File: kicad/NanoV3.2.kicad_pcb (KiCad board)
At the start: 2 copper layers, 43.2 x 17.8 mm, 24 parts, among them IC2 LM1117IMPX-5.0, IC3 ATMEGA328P-AU, P1 TTL, P2 OUT, P3 INPUT, Q1 s9014, Y1 16MHz

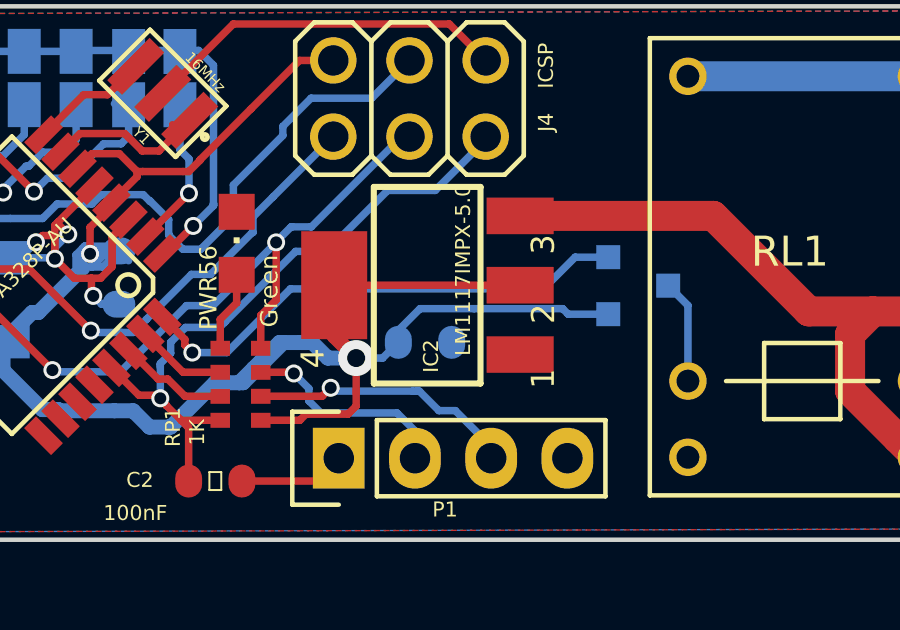
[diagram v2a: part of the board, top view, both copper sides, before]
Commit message: fixed a bug with the transistor
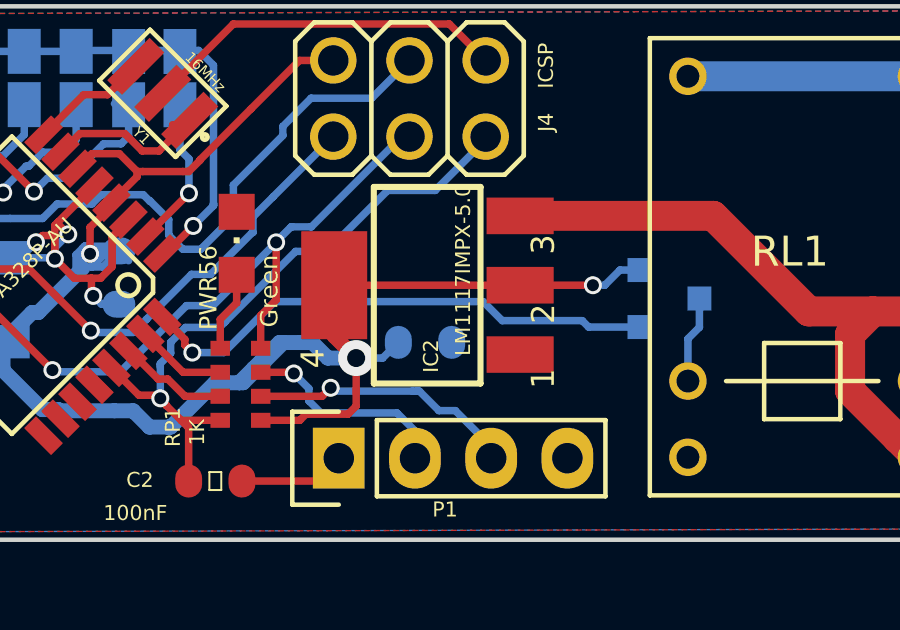
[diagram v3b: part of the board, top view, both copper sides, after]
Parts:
- Q1: value s9014 -> SS8050
- moved Q1 1.13 mm to (155.3, 105.9)
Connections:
- IC3 pad 14: /D10 -> (no net)
- IC3 pad 19: /A6 -> (no net)
- IC3 pad 22: /A7 -> (no net)
- IC3 pad 23: /A0 -> (no net)
- IC3 pad 24: /A1 -> (no net)
- IC3 pad 25: /A2 -> (no net)
- IC3 pad 26: /A3 -> (no net)
- IC3 pad 27: /A4 -> (no net)
- IC3 pad 28: /A5 -> (no net)
- Q1 pad 1: +5V -> /D2
- Q1 pad 2: /D2 -> +5V
- RL1 pad 12: Net-(RL1-Pad12) -> (no net)
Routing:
- net +5V: track 72.9 -> 69.8 mm, vias 3 -> 4
- net /D2: track 17.0 -> 17.7 mm
- net Net-(Q1-Pad3): track 3.45 -> 2.91 mm
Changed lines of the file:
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@@
     (thickness 1.6)
     (drawings 91)
-    (tracks 405)
+    (tracks 409)
     (zones 0)
     (modules 24)
-    (nets 37)
+    (nets 27)
   )
   (page A4)
@@
   (net 25 "Net-(C2-Pad2)")
   (net 26 /RX)
-  (net 27 /D10)
-  (net 28 /A6)
-  (net 29 /A7)
-  (net 30 /A0)
-  (net 31 /A1)
-  (net 32 /A2)
-  (net 33 /A3)
-  (net 34 /A4)
-  (net 35 /A5)
-  (net 36 "Net-(RL1-Pad12)")
   (net_class Default "This is the default net class."
     (clearance 0.2)
@@
     (uvia_drill 0.1)
     (add_net +5V)
-    (add_net /A0)
-    (add_net /A1)
-    (add_net /A2)
-    (add_net /A3)
-    (add_net /A4)
-    (add_net /A5)
-    (add_net /A6)
-    (add_net /A7)
     (add_net /AREF)
     (add_net /D0/RX)
     (add_net /D1/TX)
-    (add_net /D10)
     (add_net /D11/MOSI)
     (add_net /D12/MISO)
@@
     (add_net "Net-(C2-Pad2)")
     (add_net "Net-(Q1-Pad3)")
-    (add_net "Net-(RL1-Pad12)")
   )
   (net_class w0.5 ""
@@
     (pad 13 smd rect (at 0.4 4.2926 225) (size 0.5588 1.27) (layers Top F.Paste F.Mask)
       (net 21 /D9))
-    (pad 14 smd rect (at 1.2 4.2926 225) (size 0.5588 1.27) (layers Top F.Paste F.Mask)
-      (net 27 /D10))
+    (pad 14 smd rect (at 1.2 4.2926 225) (size 0.5588 1.27) (layers Top F.Paste F.Mask))
     (pad 15 smd rect (at 2 4.2926 225) (size 0.5588 1.27) (layers Top F.Paste F.Mask)
       (net 8 /D11/MOSI))
@@
     (pad 18 smd rect (at 4.2926 2 225) (size 1.27 0.5588) (layers Top F.Paste F.Mask)
       (net 2 +5V))
-    (pad 19 smd rect (at 4.2926 1.2 225) (size 1.27 0.5588) (layers Top F.Paste F.Mask)
-      (net 28 /A6))
+    (pad 19 smd rect (at 4.2926 1.2 225) (size 1.27 0.5588) (layers Top F.Paste F.Mask))
     (pad 20 smd rect (at 4.2926 0.4 225) (size 1.27 0.5588) (layers Top F.Paste F.Mask)
       (net 3 /AREF))
     (pad 21 smd rect (at 4.2926 -0.4 225) (size 1.27 0.5588) (layers Top F.Paste F.Mask)
       (net 1 COM))
-    (pad 22 smd rect (at 4.2926 -1.2 225) (size 1.27 0.5588) (layers Top F.Paste F.Mask)
-      (net 29 /A7))
-    (pad 23 smd rect (at 4.2926 -2 225) (size 1.27 0.5588) (layers Top F.Paste F.Mask)
-      (net 30 /A0))
-    (pad 24 smd rect (at 4.2926 -2.8 225) (size 1.27 0.5588) (layers Top F.Paste F.Mask)
-      (net 31 /A1))
-    (pad 25 smd rect (at 2.8 -4.2926 225) (size 0.5588 1.27) (layers Top F.Paste F.Mask)
-      (net 32 /A2))
-    (pad 26 smd rect (at 2 -4.2926 225) (size 0.5588 1.27) (layers Top F.Paste F.Mask)
-      (net 33 /A3))
-    (pad 27 smd rect (at 1.2 -4.2926 225) (size 0.5588 1.27) (layers Top F.Paste F.Mask)
-      (net 34 /A4))
-    (pad 28 smd rect (at 0.4 -4.2926 225) (size 0.5588 1.27) (layers Top F.Paste F.Mask)
-      (net 35 /A5))
+    (pad 22 smd rect (at 4.2926 -1.2 225) (size 1.27 0.5588) (layers Top F.Paste F.Mask))
+    (pad 23 smd rect (at 4.2926 -2 225) (size 1.27 0.5588) (layers Top F.Paste F.Mask))
+    (pad 24 smd rect (at 4.2926 -2.8 225) (size 1.27 0.5588) (layers Top F.Paste F.Mask))
+    (pad 25 smd rect (at 2.8 -4.2926 225) (size 0.5588 1.27) (layers Top F.Paste F.Mask))
+    (pad 26 smd rect (at 2 -4.2926 225) (size 0.5588 1.27) (layers Top F.Paste F.Mask))
+    (pad 27 smd rect (at 1.2 -4.2926 225) (size 0.5588 1.27) (layers Top F.Paste F.Mask))
+    (pad 28 smd rect (at 0.4 -4.2926 225) (size 0.5588 1.27) (layers Top F.Paste F.Mask))
     (pad 29 smd rect (at -0.4 -4.2926 225) (size 0.5588 1.27) (layers Top F.Paste F.Mask)
       (net 4 /RESET))
@@
     (pad A2 thru_hole circle (at 2.54 0 90) (size 1.25 1.25) (drill 0.762) (layers *.Cu *.Mask)
       (net 1 COM))
-    (pad 12 thru_hole circle (at 0 -7.62 90) (size 1.25 1.25) (drill 0.762) (layers *.Cu *.Mask)
-      (net 36 "Net-(RL1-Pad12)"))
+    (pad 12 thru_hole circle (at 0 -7.62 90) (size 1.25 1.25) (drill 0.762) (layers *.Cu *.Mask))
     (pad 14 thru_hole circle (at 0 0 90) (size 1.25 1.25) (drill 0.762) (layers *.Cu *.Mask)
       (net 14 VIN))
@@
   )
   (module TO_SOT_Packages_SMD:SOT-23 (layer Bottom)
-    (at 154.2288 105.42524 90)
+    (at 155.2702 105.8545 90)
     (descr "SOT-23, Standard")
     (tags SOT-23)
@@
       (effects (font (size 0.5 0.5) (thickness 0.1)) (justify mirror))
     )
-    (fp_text value s9014 (at 3.2766 -0.2794 180) (layer B.Fab)
+    (fp_text value SS8050 (at 3.2766 -0.2794 180) (layer B.Fab)
       (effects (font (size 0.5 0.5) (thickness 0.1)) (justify mirror))
     )
@@
     (fp_line (start 1.49982 0.65024) (end 1.49982 -0.0508) (layer B.SilkS) (width 0.15))
     (pad 1 smd rect (at -0.95 -1.00076 90) (size 0.8001 0.8001) (layers Bottom B.Paste B.Mask)
+      (net 22 /D2))
+    (pad 2 smd rect (at 0.95 -1.00076 90) (size 0.8001 0.8001) (layers Bottom B.Paste B.Mask)
       (net 2 +5V))
-    (pad 2 smd rect (at 0.95 -1.00076 90) (size 0.8001 0.8001) (layers Bottom B.Paste B.Mask)
-      (net 22 /D2))
     (pad 3 smd rect (at 0 0.99822 90) (size 0.8001 0.8001) (layers Bottom B.Paste B.Mask)
       (net 24 "Net-(Q1-Pad3)"))
@@
   (segment (start 163.50488 108.60532) (end 167.3098 108.60532) (width 0.25) (layer Bottom) (net 1))
   (segment (start 167.3098 108.60532) (end 167.52824 108.82376) (width 0.25) (layer Bottom) (net 1))
+  (segment (start 152.7175 105.41) (end 150.2918 105.41) (width 0.25) (layer Top) (net 2))
+  (segment (start 153.11389 105.41) (end 152.7175 105.41) (width 0.25) (layer Bottom) (net 2))
+  (via (at 152.7175 105.41) (size 0.6) (drill 0.4) (layers Top Bottom) (net 2))
+  (segment (start 154.26944 104.9045) (end 153.61939 104.9045) (width 0.25) (layer Bottom) (net 2))
+  (segment (start 153.61939 104.9045) (end 153.11389 105.41) (width 0.25) (layer Bottom) (net 2))
+  (segment (start 146.23288 107.4158) (end 146.23288 107.315) (width 0.25) (layer Bottom) (net 2))
   (segment (start 140.92936 108.6612) (end 141.05636 108.6612) (width 0.5) (layer Bottom) (net 2))
   (segment (start 141.05636 108.6612) (end 141.53388 108.18368) (width 0.5) (layer Bottom) (net 2))
@@
   (segment (start 137.93724 110.13948) (end 138.557 110.13948) (width 0.5) (layer Bottom) (net 2))
   (segment (start 133.05536 108.27004) (end 133.05536 107.2896) (width 0.5) (layer Bottom) (net 2))
-  (segment (start 148.76272 106.19232) (end 151.70904 106.19232) (width 0.25) (layer Bottom) (net 2))
-  (segment (start 151.70904 106.19232) (end 151.89196 106.37524) (width 0.25) (layer Bottom) (net 2))
   (segment (start 146.23288 107.315) (end 146.23288 106.91368) (width 0.25) (layer Bottom) (net 2))
-  (segment (start 146.23288 106.91368) (end 146.95424 106.19232) (width 0.25) (layer Bottom) (net 2))
-  (segment (start 151.89196 106.37524) (end 153.22804 106.37524) (width 0.25) (layer Bottom) (net 2))
-  (segment (start 146.95424 106.19232) (end 148.76272 106.19232) (width 0.25) (layer Bottom) (net 2))
   (segment (start 144.82572 107.83824) (end 145.70964 107.83824) (width 0.25) (layer Bottom) (net 2))
   (segment (start 145.70964 107.83824) (end 146.23288 107.315) (width 0.25) (layer Bottom) (net 2))
@@
   (segment (start 128.63576 100.64496) (end 128.63576 101.261445) (width 0.25) (layer Top) (net 21))
   (segment (start 128.63576 101.261445) (end 130.031831 102.657516) (width 0.25) (layer Top) (net 21))
-  (segment (start 153.22804 104.47524) (end 152.12572 104.47524) (width 0.25) (layer Bottom) (net 22))
+  (segment (start 152.3619 106.5911) (end 152.5753 106.8045) (width 0.25) (layer Bottom) (net 22))
+  (segment (start 152.5753 106.8045) (end 154.26944 106.8045) (width 0.25) (layer Bottom) (net 22))
+  (segment (start 149.6949 106.5911) (end 152.3619 106.5911) (width 0.25) (layer Bottom) (net 22))
+  (segment (start 149.0599 105.9561) (end 149.6949 106.5911) (width 0.25) (layer Bottom) (net 22))
+  (segment (start 142.113 105.9561) (end 149.0599 105.9561) (width 0.25) (layer Bottom) (net 22))
+  (segment (start 142.113 105.9561) (end 140.41374 107.65536) (width 0.25) (layer Bottom) (net 22))
+  (segment (start 140.41374 107.65536) (end 139.36472 107.65536) (width 0.25) (layer Bottom) (net 22))
   (segment (start 139.1158 107.216002) (end 138.365226 106.465428) (width 0.25) (layer Top) (net 22))
   (segment (start 139.1158 107.40644) (end 139.1158 107.216002) (width 0.25) (layer Top) (net 22))
   (segment (start 139.36472 107.65536) (end 139.1158 107.40644) (width 0.25) (layer Top) (net 22))
   (via (at 139.36472 107.65536) (size 0.6) (drill 0.4) (layers Top Bottom) (net 22))
-  (segment (start 140.5128 107.65536) (end 139.36472 107.65536) (width 0.25) (layer Bottom) (net 22))
-  (segment (start 142.63624 105.53192) (end 140.5128 107.65536) (width 0.25) (layer Bottom) (net 22))
-  (segment (start 151.06904 105.53192) (end 142.63624 105.53192) (width 0.25) (layer Bottom) (net 22))
-  (segment (start 152.12572 104.47524) (end 151.06904 105.53192) (width 0.25) (layer Bottom) (net 22))
   (segment (start 138.365226 106.465428) (end 138.365226 106.569506) (width 0.25) (layer Top) (net 22))
   (segment (start 138.365226 106.544106) (end 138.365226 106.465428) (width 0.25) (layer Top) (net 22))
@@
   (segment (start 165.5572 98.44532) (end 167.52824 100.41636) (width 0.5) (layer Bottom) (net 23))
   (segment (start 165.5572 98.44532) (end 167.52824 100.41636) (width 0.25) (layer Bottom) (net 23))
-  (segment (start 155.88488 108.60532) (end 155.88488 106.0831) (width 0.25) (layer Bottom) (net 24))
-  (segment (start 155.88488 106.0831) (end 155.22702 105.42524) (width 0.25) (layer Bottom) (net 24))
+  (segment (start 156.26842 106.81208) (end 155.88488 107.19562) (width 0.25) (layer Bottom) (net 24))
+  (segment (start 155.88488 107.19562) (end 155.88488 108.60532) (width 0.25) (layer Bottom) (net 24))
+  (segment (start 156.26842 105.8545) (end 156.26842 106.81208) (width 0.25) (layer Bottom) (net 24))
   (segment (start 141.01826 111.9378) (end 143.4846 111.9378) (width 0.25) (layer Top) (net 25))
   (segment (start 143.4846 111.9378) (end 144.2466 111.1758) (width 0.25) (layer Top) (net 25))
